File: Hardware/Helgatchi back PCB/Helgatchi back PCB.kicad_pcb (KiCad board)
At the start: 2 copper layers, 50 x 80 mm, 9 parts, among them J1 u.FL, J2 RP-SMA

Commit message: Drawings and laser cutter files
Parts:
- added kibuzzard-6984DC4B: G***, kibuzzard-6984DC4B, B.Cu at (153.5, 34.5)
- added kibuzzard-6984DC6C: G***, kibuzzard-6984DC6C, B.Cu at (139.8, 44.0)
- H1, H2: footprint MountingHole:MountingHole_2.2mm_M2_Pad_Via -> MountingHole:MountingHole_2.2mm_M2_Pad
- J2: footprint Connector_Coaxial:SMA_Samtec_SMA-J-P-H-ST-EM1_EdgeMount -> Connector_Coaxial:SMA_Amphenol_901-143_Horizontal
- moved J1 15.0 mm to (145.0, 44.0)
- moved J2 1.34 mm to (145.0, 34.5), turned to 180 degrees
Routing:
- net Net-(J1-In): track 24.4 -> 8.00 mm
- net GND: vias 75 -> 23
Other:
- outline, holes or cut-outs redrawn
- board text removed: "2.4GHz ANTENNA"

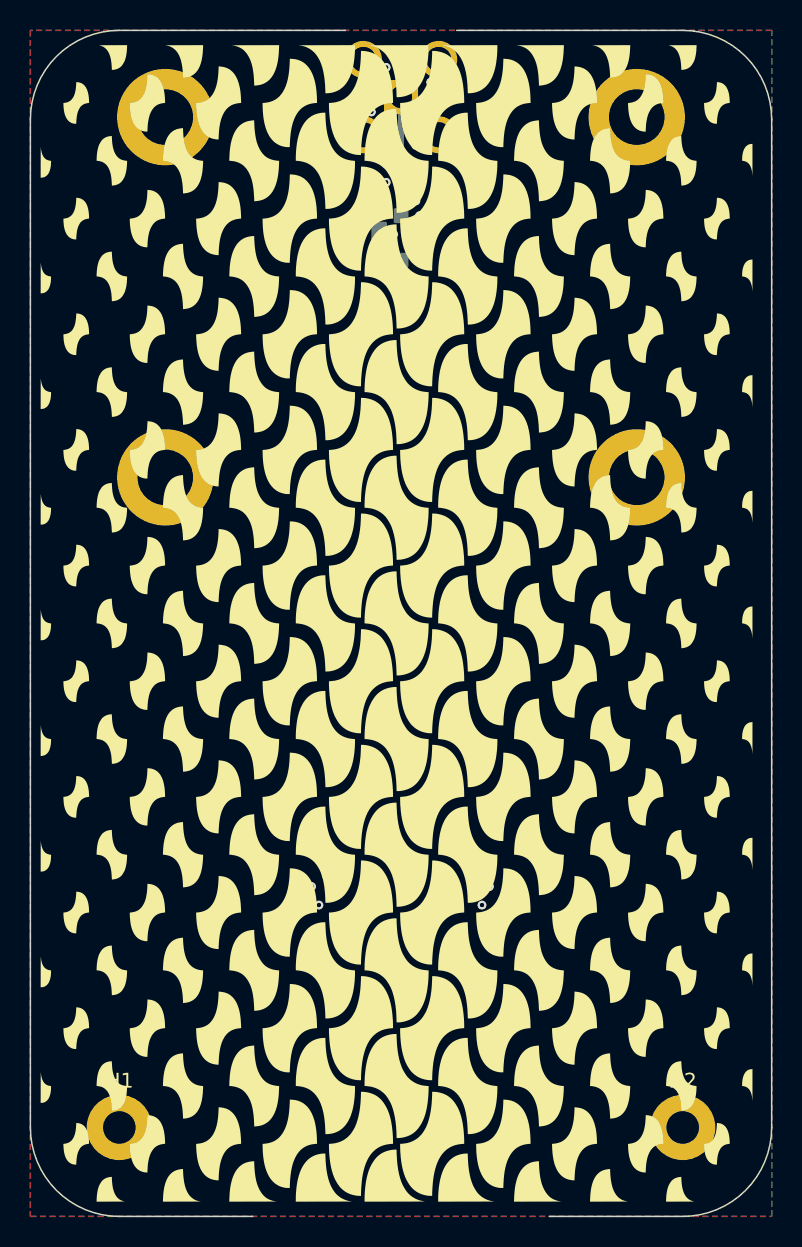
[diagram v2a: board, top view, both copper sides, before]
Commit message: Update back PCB to R2.7
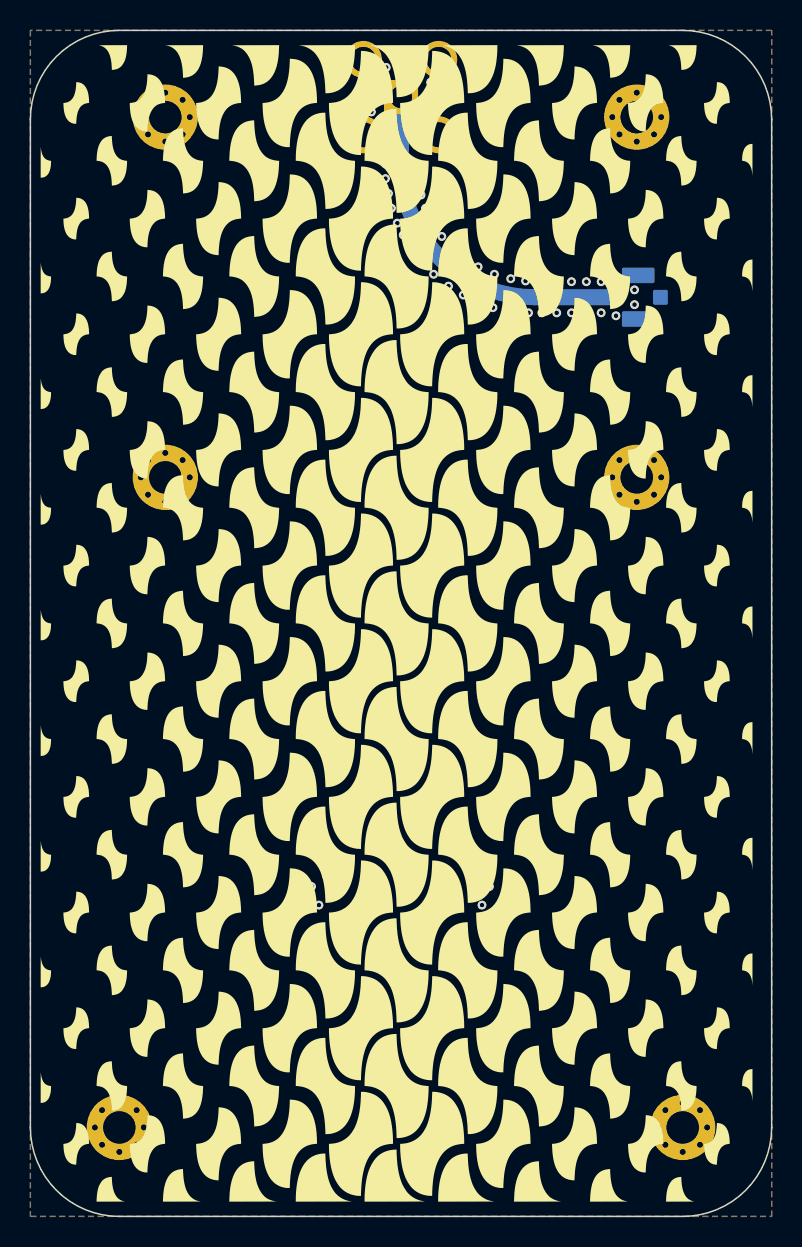
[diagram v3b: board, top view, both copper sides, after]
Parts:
- removed kibuzzard-6984DC4B: G***, kibuzzard-6984DC4B
- removed kibuzzard-6984DC6C: G***, kibuzzard-6984DC6C
- added G***: LOGO, LOGO, B.Cu at (144.5, 47.2)
- added G***: LOGO, LOGO, B.Cu at (136.0, 75.5)
- added G***: LOGO, LOGO, B.Cu at (145.5, 48.3)
- added G***: LOGO, LOGO, B.Cu at (154.0, 77.0)
- added kibuzzard-69B731C5: G***, kibuzzard-69B731C5, B.Cu at (161.0, 44.5)
- added kibuzzard-69B731D4: G***, kibuzzard-69B731D4, B.Cu at (145.0, 40.0)
- added kibuzzard-69B73206: G***, kibuzzard-69B73206, B.Cu at (144.5, 51.2)
- added kibuzzard-69B73420: G***, kibuzzard-69B73420, B.Cu at (154.0, 69.0)
- added kibuzzard-69B73430: G***, kibuzzard-69B73430, B.Cu at (136.0, 69.0)
- added kibuzzard-69B735E8: G***, kibuzzard-69B735E8, B.Cu at (145.0, 85.0)
- added kibuzzard-69B7363E: G***, kibuzzard-69B7363E, B.Cu at (145.0, 57.0)
- H1, H2: footprint MountingHole:MountingHole_2.2mm_M2_Pad -> MountingHole:MountingHole_2.2mm_M2_Pad_Via
- H3, H4, H5, H6: footprint Sinhoo SMTSO 2M:SMTSO M2 solder pad -> MountingHole:MountingHole_2.2mm_M2_Pad_Via
- moved J1 16.5 mm to (161.0, 48.0), turned to 90 degrees
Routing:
- net Net-(J1-In): track 8.00 -> 10.0 mm
- net GND: vias 23 -> 54
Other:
- outline, holes or cut-outs redrawn
- board text added: "Netkisune Poly801 kimb3r n1ghtbl00d Wade & Cade Person1 Person2 Person3 Person4 Person5"
- board text removed: "CREDITS"
- board text removed: "Netkisune Poly801 kimb3r n1ghtbl00d Wade"

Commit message: Update to new firmware
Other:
- board text added: "SamIAm Tucker MKFactor kimb3r Netkisune Wade & Cade Poly801 n1ghtbl00d"
- board text removed: "Netkisune Poly801 kimb3r n1ghtbl00d Wade & Cade Person1 Person2 Person3 Person4 Person5"
